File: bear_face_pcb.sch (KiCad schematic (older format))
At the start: 199 parts, among them J1 USB_B_Micro-Connector, J2 Conn_02x03_Odd_Even, SW1 RESET, U1 ATmega32U4-AU, U2 SRV05-4, Y1 16MHz

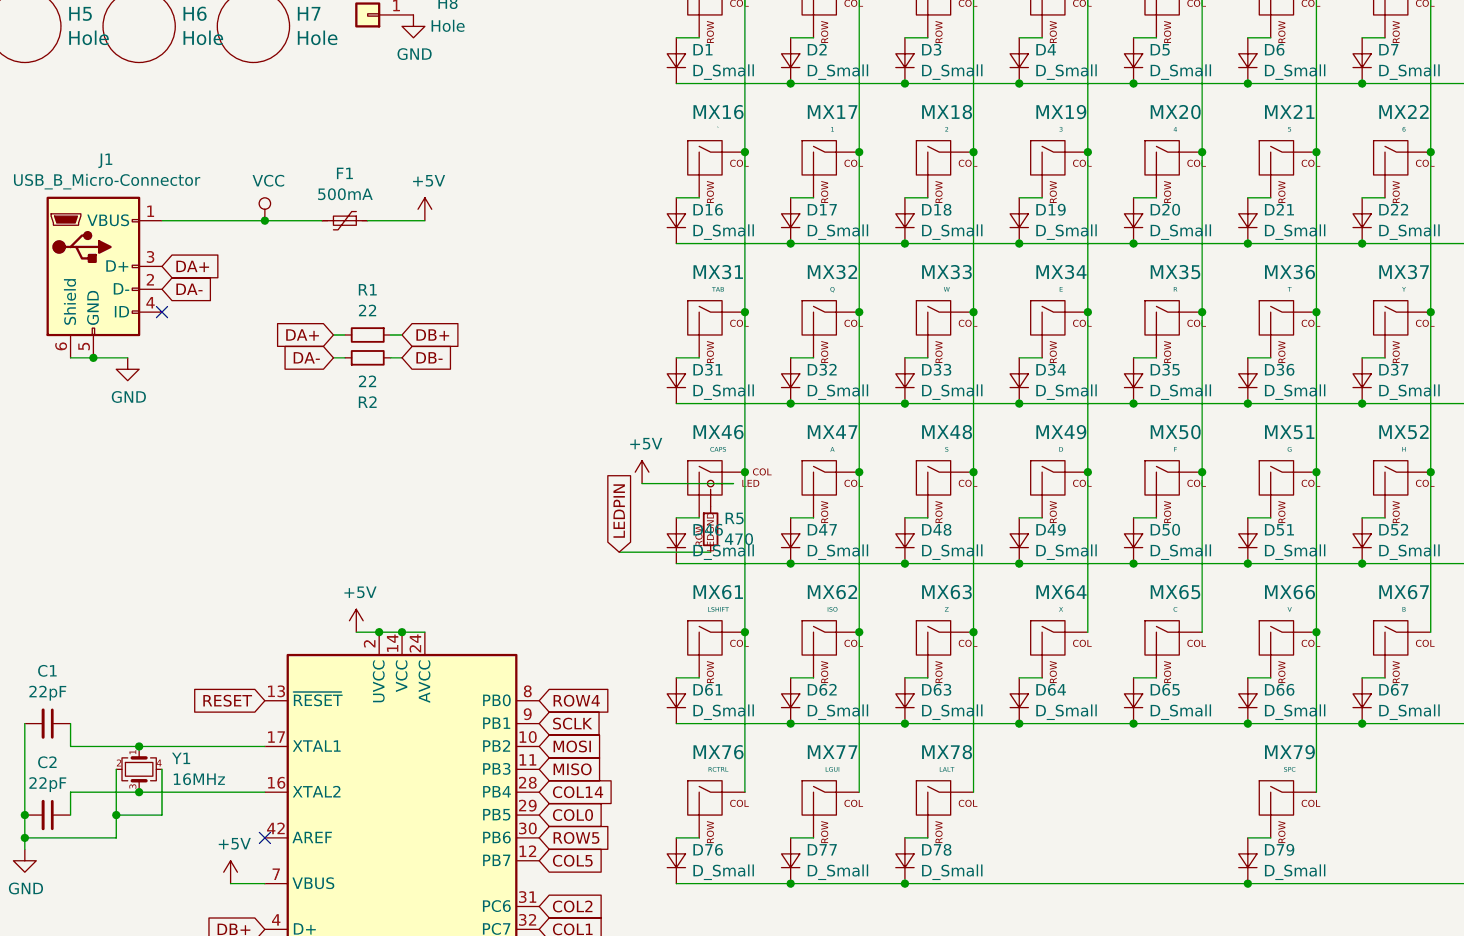
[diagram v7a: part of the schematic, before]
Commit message: standardized footprints, moved USB, moved silks * 'professionalized' * deleted old gerbers * RESET switch looks much nicer
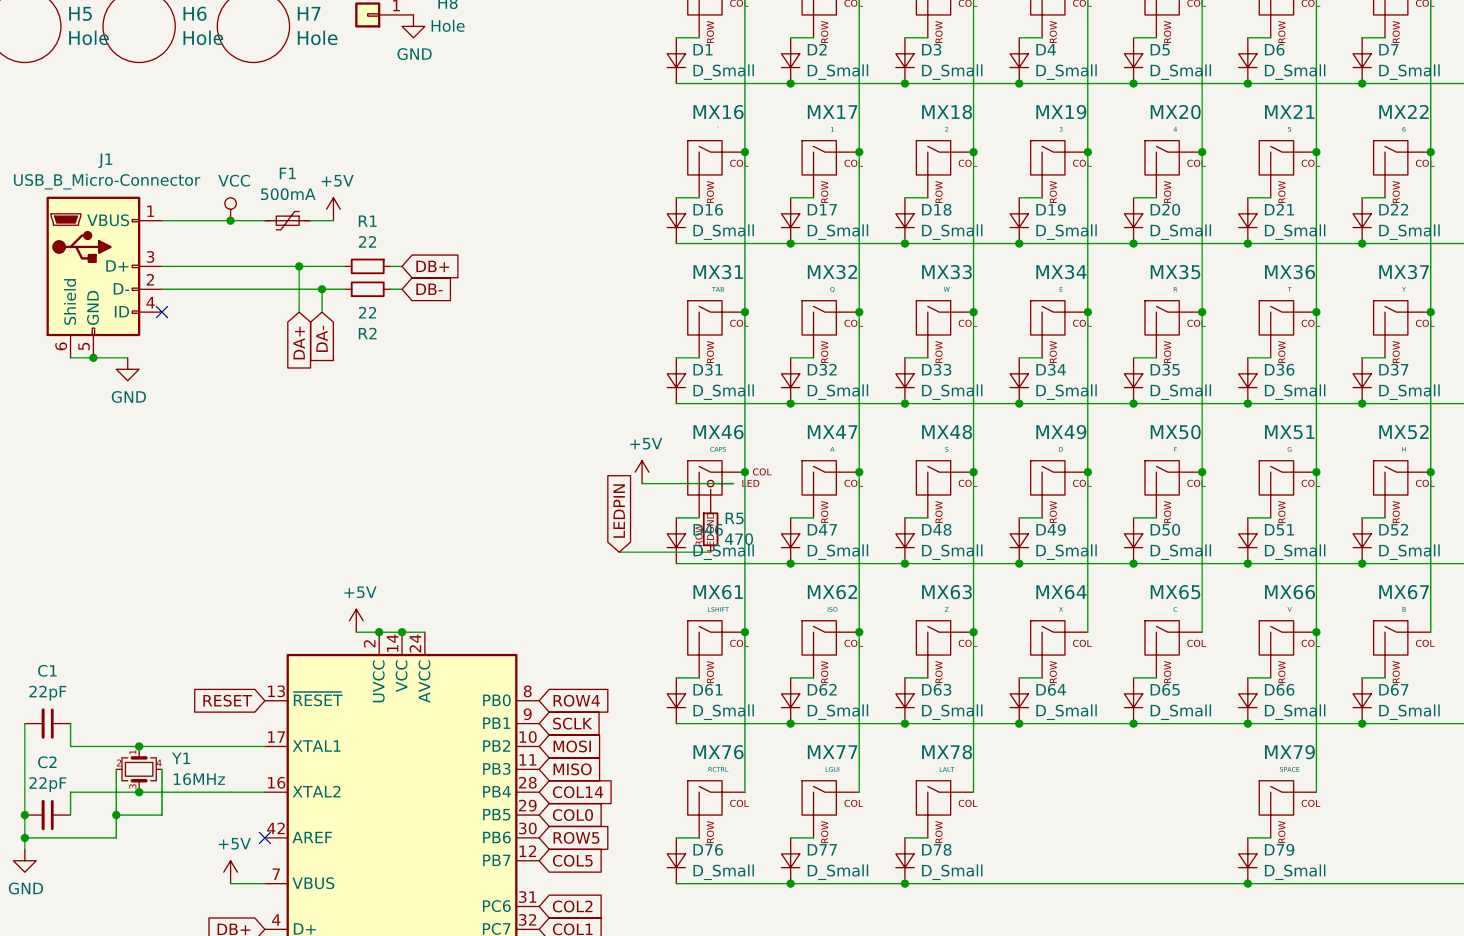
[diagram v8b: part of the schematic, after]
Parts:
- MX79: value SPC -> SPACE
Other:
- moved on the sheet: F1, R1, R2
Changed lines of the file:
@@
 P 6200 4600
 F 0 "MX79" H 6233 4823 60  0000 C CNN
-F 1 "SPC" H 6233 4749 20  0000 C CNN
+F 1 "SPACE" H 6233 4749 20  0000 C CNN
 F 2 "bear_face_parts:MXOnly-6.25U-NoLED-NoStabs" H 5575 4575 60  0001 C CNN
 F 3 "" H 5575 4575 60  0001 C CNN
@@
 L power:+5V #PWR03
 U 1 1 5E226273
-P 2450 2050
-F 0 "#PWR03" H 2450 1900 50  0001 C CNN
-F 1 "+5V" H 2465 2223 50  0000 C CNN
-F 2 "" H 2450 2050 50  0001 C CNN
-F 3 "" H 2450 2050 50  0001 C CNN
-	1    2450 2050
+P 2050 2050
+F 0 "#PWR03" H 2050 1900 50  0001 C CNN
+F 1 "+5V" H 2065 2223 50  0000 C CNN
+F 2 "" H 2050 2050 50  0001 C CNN
+F 3 "" H 2050 2050 50  0001 C CNN
+	1    2050 2050
 	1    0    0    -1
 $EndComp
@@
 L Device:Polyfuse_Small F1
 U 1 1 5E21E2B0
-P 2100 2050
-F 0 "F1" V 1895 2050 50  0000 C CNN
-F 1 "500mA" V 1986 2050 50  0000 C CNN
-F 2 "Fuse:Fuse_1206_3216Metric" H 2150 1850 50  0001 L CNN
-F 3 "~" H 2100 2050 50  0001 C CNN
-F 4 "C70076" V 2100 2050 50  0001 C CNN "LCSC"
-	1    2100 2050
+P 1850 2050
+F 0 "F1" V 1645 2050 50  0000 C CNN
+F 1 "500mA" V 1736 2050 50  0000 C CNN
+F 2 "Fuse:Fuse_1206_3216Metric" H 1900 1850 50  0001 L CNN
+F 3 "~" H 1850 2050 50  0001 C CNN
+F 4 "C70076" V 1850 2050 50  0001 C CNN "LCSC"
+	1    1850 2050
 	0    1    1    0
 $EndComp
@@
 L Device:R_Small R1
 U 1 1 66036275
-P 2200 2550
-F 0 "R1" V 2004 2550 50  0000 C CNN
-F 1 "22" V 2095 2550 50  0000 C CNN
-F 2 "Resistor_SMD:R_0805_2012Metric" H 2200 2550 50  0001 C CNN
-F 3 "~" H 2200 2550 50  0001 C CNN
-F 4 "C17561" V 2200 2550 50  0001 C CNN "LCSC"
-	1    2200 2550
+P 2200 2250
+F 0 "R1" V 2004 2250 50  0000 C CNN
+F 1 "22" V 2095 2250 50  0000 C CNN
+F 2 "Resistor_SMD:R_0805_2012Metric" H 2200 2250 50  0001 C CNN
+F 3 "~" H 2200 2250 50  0001 C CNN
+F 4 "C17561" V 2200 2250 50  0001 C CNN "LCSC"
+	1    2200 2250
 	0    1    1    0
 $EndComp
@@
 L Device:R_Small R2
 U 1 1 66037A5E
-P 2200 2650
-F 0 "R2" V 2004 2650 50  0000 C CNN
-F 1 "22" V 2095 2650 50  0000 C CNN
-F 2 "Resistor_SMD:R_0805_2012Metric" H 2200 2650 50  0001 C CNN
-F 3 "~" H 2200 2650 50  0001 C CNN
-F 4 "C17561" V 2200 2650 50  0001 C CNN "LCSC"
-	1    2200 2650
+P 2200 2350
+F 0 "R2" V 2004 2350 50  0000 C CNN
+F 1 "22" V 2095 2350 50  0000 C CNN
+F 2 "Resistor_SMD:R_0805_2012Metric" H 2200 2350 50  0001 C CNN
+F 3 "~" H 2200 2350 50  0001 C CNN
+F 4 "C17561" V 2200 2350 50  0001 C CNN "LCSC"
+	1    2200 2350
 	0    -1   -1   0
 $EndComp
@@
 L power:VCC #PWR02
 U 1 1 5E224EBD
-P 1750 2050
-F 0 "#PWR02" H 1750 1900 50  0001 C CNN
-F 1 "VCC" H 1767 2223 50  0000 C CNN
-F 2 "" H 1750 2050 50  0001 C CNN
-F 3 "" H 1750 2050 50  0001 C CNN
-	1    1750 2050
-	1    0    0    -1
-$EndComp
-Text GLabel 1300 2350 2    50   Input ~ 0
+P 1600 2050
+F 0 "#PWR02" H 1600 1900 50  0001 C CNN
+F 1 "VCC" H 1617 2223 50  0000 C CNN
+F 2 "" H 1600 2050 50  0001 C CNN
+F 3 "" H 1600 2050 50  0001 C CNN
+	1    1600 2050
+	1    0    0    -1
+$EndComp
+Text GLabel 2000 2450 3    50   Input ~ 0
 DA-
-Text GLabel 1300 2250 2    50   Input ~ 0
+Text GLabel 1900 2450 3    50   Input ~ 0
 DA+
-Text GLabel 2350 2650 2    50   Input ~ 0
+Text GLabel 2350 2350 2    50   Input ~ 0
 DB-
-Text GLabel 2350 2550 2    50   Input ~ 0
+Text GLabel 2350 2250 2    50   Input ~ 0
 DB+
-$Comp
-L bear_face_pcb:USB_B_Micro-Connector J1
-U 1 1 6554DB7C
-P 1000 2250
-F 0 "J1" H 1057 2717 50  0000 C CNN
-F 1 "USB_B_Micro-Connector" H 1057 2626 50  0000 C CNN
-F 2 "Connector_USB:USB_Micro-B_Wuerth_629105150521" H 1150 2200 50  0001 C CNN
-F 3 "" H 1150 2200 50  0001 C CNN
-	1    1000 2250
-	1    0    0    -1
-$EndComp
-Wire Wire Line
-	1300 2050 1750 2050
-Wire Wire Line
-	2200 2050 2450 2050
-Connection ~ 1750 2050
-Wire Wire Line
-	1750 2050 2000 2050
 NoConn ~ 1300 2450
 Wire Wire Line
@@
 $EndComp
 Wire Wire Line
-	2300 2550 2350 2550
-Wire Wire Line
-	2300 2650 2350 2650
-Text GLabel 2050 2550 0    50   Input ~ 0
-DA+
-Text GLabel 2050 2650 0    50   Input ~ 0
-DA-
-Wire Wire Line
-	2050 2550 2100 2550
-Wire Wire Line
-	2050 2650 2100 2650
+	2300 2250 2350 2250
+Wire Wire Line
+	2300 2350 2350 2350
+$Comp
+L bear_face_pcb:USB_B_Micro-Connector J1
+U 1 1 6554DB7C
+P 1000 2250
+F 0 "J1" H 1057 2717 50  0000 C CNN
+F 1 "USB_B_Micro-Connector" H 1057 2626 50  0000 C CNN
+F 2 "Connector_USB:USB_Micro-B_Wuerth_629105150521" H 1150 2200 50  0001 C CNN
+F 3 "" H 1150 2200 50  0001 C CNN
+F 4 "" H 1000 2250 50  0001 C CNN "LCSC"
+	1    1000 2250
+	1    0    0    -1
+$EndComp
+Wire Wire Line
+	1300 2050 1600 2050
+Wire Wire Line
+	1600 2050 1750 2050
+Connection ~ 1600 2050
+Wire Wire Line
+	1950 2050 2050 2050
+Wire Wire Line
+	1300 2250 1900 2250
+Wire Wire Line
+	1300 2350 2000 2350
+Wire Wire Line
+	2000 2450 2000 2350
+Connection ~ 2000 2350
+Wire Wire Line
+	2000 2350 2100 2350
+Wire Wire Line
+	1900 2450 1900 2250
+Connection ~ 1900 2250
+Wire Wire Line
+	1900 2250 2100 2250
 $EndSCHEMATC
